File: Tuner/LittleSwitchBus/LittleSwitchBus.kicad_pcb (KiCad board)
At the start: 2 copper layers, 100 x 100 mm, 101 parts, among them J1 Conn_Coaxial, J10 Conn_Coaxial, J11 Conn_02x05_Odd_Even, J13 Conn_01x01, J14 Conn_01x01, J15 Conn_01x01, J16 Conn_01x01, J2 Conn_Coaxial, J3 Conn_Coaxial, J4 Conn_Coaxial, J5 Conn_Coaxial, J6 Conn_Coaxial, J7 Conn_Coaxial, J8 Conn_Coaxial, J9 Conn_Coaxial, U1 MCP23008, U2 ULN2803A

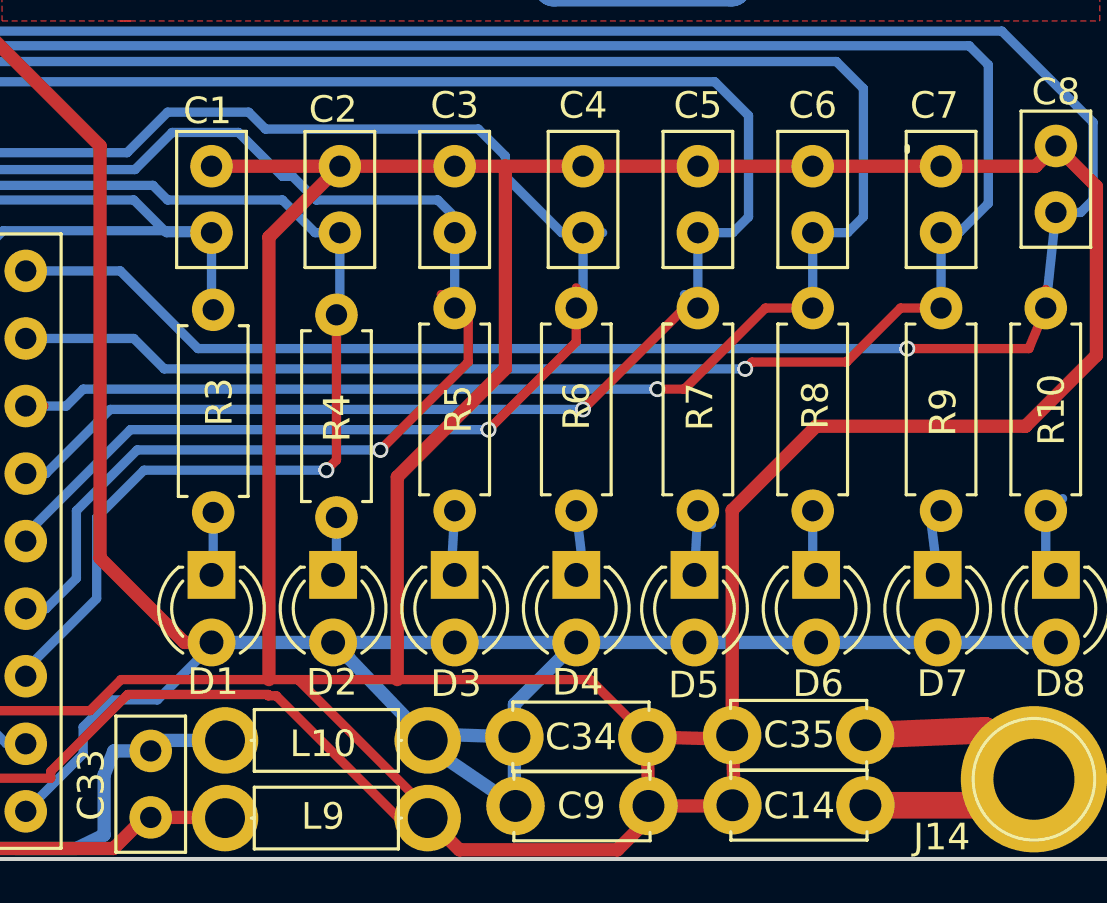
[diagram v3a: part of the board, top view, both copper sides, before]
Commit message: Added yet more ground connections
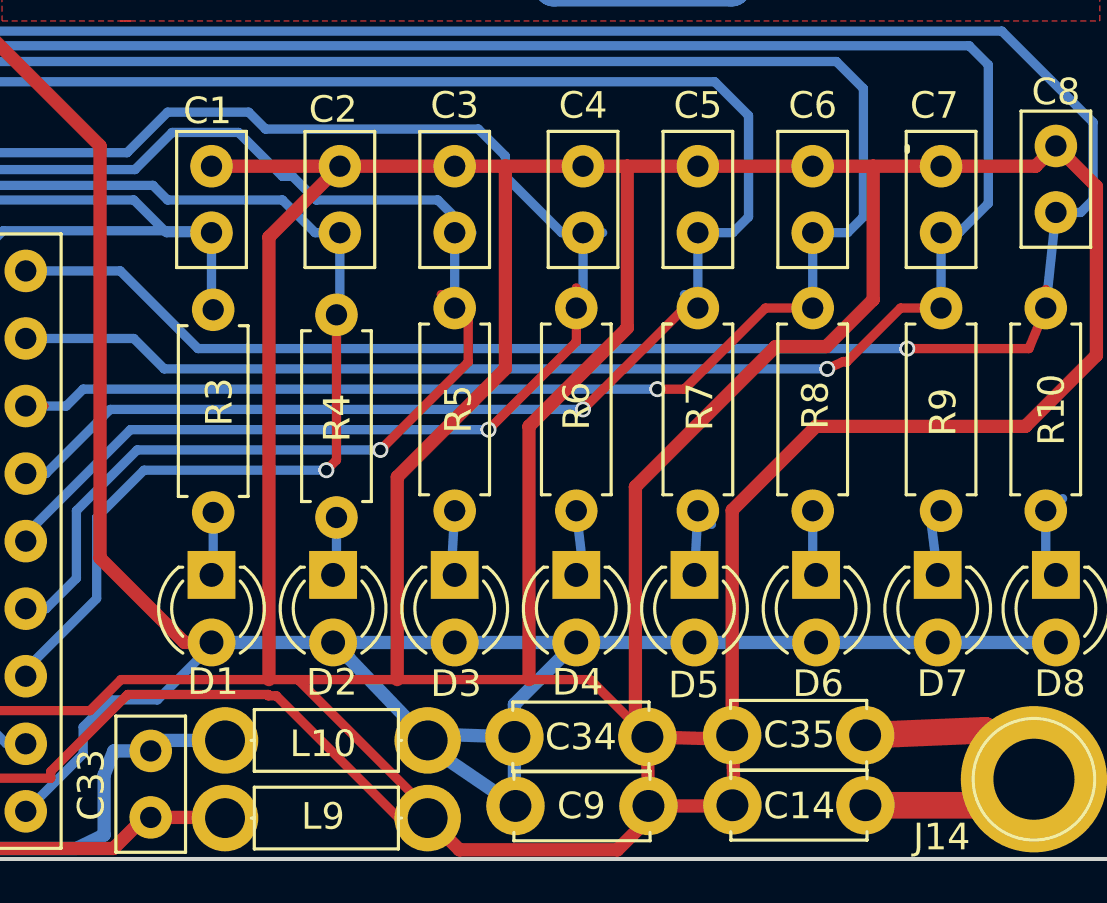
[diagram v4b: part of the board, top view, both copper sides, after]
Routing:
- net RLYGND: track 201.2 -> 248.5 mm
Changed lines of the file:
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@@
     (thickness 1.6)
     (drawings 27)
-    (tracks 895)
+    (tracks 907)
     (zones 0)
     (modules 101)
@@
   (gr_line (start 150 150) (end 50 150) (angle 90) (layer Edge.Cuts) (width 0.15))
   (gr_line (start 50 50) (end 150 50) (angle 90) (layer Edge.Cuts) (width 0.15))
-  (segment (start 93.726 54.864) (end 89.154 54.864) (width 0.5) (layer F.Cu) (net 1) (status 400000))
+  (segment (start 93.726 54.864) (end 89.154 54.864) (width 0.5) (layer F.Cu) (net 1))
   (segment (start 89.154 54.864) (end 88.9 55.118) (width 0.5) (layer F.Cu) (net 1))
   (segment (start 53.803 52.197) (end 53 53) (width 1) (layer F.Cu) (net 1) (status 30))
@@
   (segment (start 141.986 129.286) (end 143.51 129.286) (width 0.35) (layer F.Cu) (net 17) (status 20))
   (segment (start 139.954 131.318) (end 141.986 129.286) (width 0.35) (layer F.Cu) (net 17))
-  (segment (start 136.398 131.318) (end 139.954 131.318) (width 0.35) (layer F.Cu) (net 17))
-  (segment (start 136.144 131.572) (end 136.398 131.318) (width 0.35) (layer F.Cu) (net 17))
-  (via (at 136.144 131.572) (size 0.6) (drill 0.4) (layers F.Cu B.Cu) (net 17))
-  (segment (start 114.3 131.572) (end 136.144 131.572) (width 0.35) (layer B.Cu) (net 17))
+  (segment (start 139.8397 131.2926) (end 139.954 131.318) (width 0.35) (layer F.Cu) (net 17))
+  (segment (start 139.2301 131.572) (end 139.8397 131.2926) (width 0.35) (layer F.Cu) (net 17))
+  (via (at 139.2301 131.572) (size 0.6) (drill 0.4) (layers F.Cu B.Cu) (net 17))
+  (segment (start 114.3 131.572) (end 139.2301 131.572) (width 0.35) (layer B.Cu) (net 17))
   (segment (start 113.157 130.429) (end 114.3 131.572) (width 0.35) (layer B.Cu) (net 17))
   (segment (start 143.51 126.452) (end 143.51 129.286) (width 0.35) (layer B.Cu) (net 17) (status 30))
@@
   (segment (start 148.463 138.684) (end 147.828 139.319) (width 0.35) (layer B.Cu) (net 30) (status 30))
   (segment (start 147.9296 136.6012) (end 148.082 136.4488) (width 0.35) (layer B.Cu) (net 30) (status 30))
+  (segment (start 131.7117 123.952) (end 131.7117 130.0353) (width 0.5) (layer F.Cu) (net 31))
+  (segment (start 128.016 133.731) (end 128.016 143.256) (width 0.5) (layer F.Cu) (net 31))
+  (segment (start 131.7117 130.0353) (end 128.016 133.731) (width 0.5) (layer F.Cu) (net 31))
+  (segment (start 140.9573 123.952) (end 140.9573 128.9685) (width 0.5) (layer F.Cu) (net 31))
+  (segment (start 132.0165 136.0043) (end 132.0165 144.95906) (width 0.5) (layer F.Cu) (net 31))
+  (segment (start 137.287 130.7338) (end 132.0165 136.0043) (width 0.5) (layer F.Cu) (net 31))
+  (segment (start 139.192 130.7338) (end 137.287 130.7338) (width 0.5) (layer F.Cu) (net 31))
+  (segment (start 140.9573 128.9685) (end 139.192 130.7338) (width 0.5) (layer F.Cu) (net 31))
+  (segment (start 132.0165 144.95906) (end 132.46736 145.40992) (width 0.5) (layer F.Cu) (net 31))
   (segment (start 135.65504 145.34896) (end 135.65504 136.88696) (width 0.5) (layer F.Cu) (net 31))
   (segment (start 149.352 124.714) (end 147.828 123.19) (width 0.5) (layer F.Cu) (net 31))
@@
   (segment (start 118.237 143.256) (end 118.237 126.619) (width 0.5) (layer F.Cu) (net 31))
   (segment (start 118.237 126.619) (end 120.904 123.952) (width 0.5) (layer F.Cu) (net 31))
-  (segment (start 138.684 123.952) (end 143.51 123.952) (width 0.5) (layer F.Cu) (net 31))
+  (segment (start 138.684 123.952) (end 140.9573 123.952) (width 0.5) (layer F.Cu) (net 31))
+  (segment (start 140.9573 123.952) (end 143.51 123.952) (width 0.5) (layer F.Cu) (net 31))
   (segment (start 143.51 123.952) (end 147.066 123.952) (width 0.5) (layer F.Cu) (net 31))
   (segment (start 147.066 123.952) (end 147.828 123.19) (width 0.5) (layer F.Cu) (net 31))
   (segment (start 119.3292 143.256) (end 123.063 143.256) (width 0.35) (layer F.Cu) (net 31))
-  (segment (start 123.063 143.256) (end 130.31344 143.256) (width 0.35) (layer F.Cu) (net 31))
+  (segment (start 123.063 143.256) (end 128.016 143.256) (width 0.35) (layer F.Cu) (net 31))
+  (segment (start 128.016 143.256) (end 130.31344 143.256) (width 0.35) (layer F.Cu) (net 31))
   (segment (start 130.31344 143.256) (end 132.46736 145.40992) (width 0.35) (layer F.Cu) (net 31) (status 20))
   (segment (start 118.2116 143.8656) (end 118.5164 143.8656) (width 0.35) (layer F.Cu) (net 31))
@@
   (segment (start 112.9284 143.8148) (end 118.2116 143.8148) (width 0.35) (layer F.Cu) (net 31))
   (segment (start 134.366 123.952) (end 138.684 123.952) (width 0.5) (layer F.Cu) (net 31) (status 30))
-  (segment (start 130.048 123.952) (end 134.366 123.952) (width 0.5) (layer F.Cu) (net 31) (status 30))
+  (segment (start 130.048 123.952) (end 131.7117 123.952) (width 0.5) (layer F.Cu) (net 31) (status 30))
+  (segment (start 131.7117 123.952) (end 134.366 123.952) (width 0.5) (layer F.Cu) (net 31) (status 30))
   (segment (start 125.222 123.952) (end 127.127 123.952) (width 0.5) (layer F.Cu) (net 31) (status 30))
   (segment (start 127.127 123.952) (end 130.048 123.952) (width 0.5) (layer F.Cu) (net 31) (status 30))
@@
   (segment (start 123.4821 148.1709) (end 123.4821 147.7899) (width 0.35) (layer F.Cu) (net 31) (status 30))
   (segment (start 101.854 65.659) (end 101.854 61.214) (width 0.5) (layer F.Cu) (net 32))
-  (segment (start 103.886 58.888) (end 105.918 56.856) (width 0.5) (layer F.Cu) (net 32) (status 800000))
+  (segment (start 103.886 58.888) (end 105.918 56.856) (width 0.5) (layer F.Cu) (net 32))
   (segment (start 103.886 59.182) (end 103.886 58.888) (width 0.5) (layer F.Cu) (net 32))
   (segment (start 101.854 61.214) (end 103.886 59.182) (width 0.5) (layer F.Cu) (net 32))
-  (segment (start 93.726 57.364) (end 93.726 59.794) (width 0.5) (layer F.Cu) (net 32) (status 400000))
-  (segment (start 93.726 59.794) (end 92.931 60.589) (width 0.5) (layer F.Cu) (net 32) (status 800000))
+  (segment (start 93.726 57.364) (end 93.726 59.794) (width 0.5) (layer F.Cu) (net 32))
+  (segment (start 93.726 59.794) (end 92.931 60.589) (width 0.5) (layer F.Cu) (net 32))
   (segment (start 116.078 141.859) (end 115.062 141.859) (width 0.5) (layer F.Cu) (net 32))
   (segment (start 111.887 123.19) (end 106.84 118.143) (width 0.5) (layer F.Cu) (net 32))
@@
   (segment (start 128.524 93.726) (end 130.81 96.012) (width 1.5) (layer B.Cu) (net 55))
   (segment (start 114.46 88.91) (end 114.46 92.456) (width 1.5) (layer B.Cu) (net 55))
-  (segment (start 105.918 54.356) (end 108.712 54.356) (width 0.5) (layer F.Cu) (net 56) (status 400000))
+  (segment (start 105.918 54.356) (end 108.712 54.356) (width 0.5) (layer F.Cu) (net 56))
   (segment (start 108.712 54.356) (end 108.966 54.61) (width 0.5) (layer F.Cu) (net 56))
   (segment (start 128.082 77.978) (end 128.524 77.978) (width 1.5) (layer B.Cu) (net 57))
